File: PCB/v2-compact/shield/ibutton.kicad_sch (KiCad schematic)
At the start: 0 parts

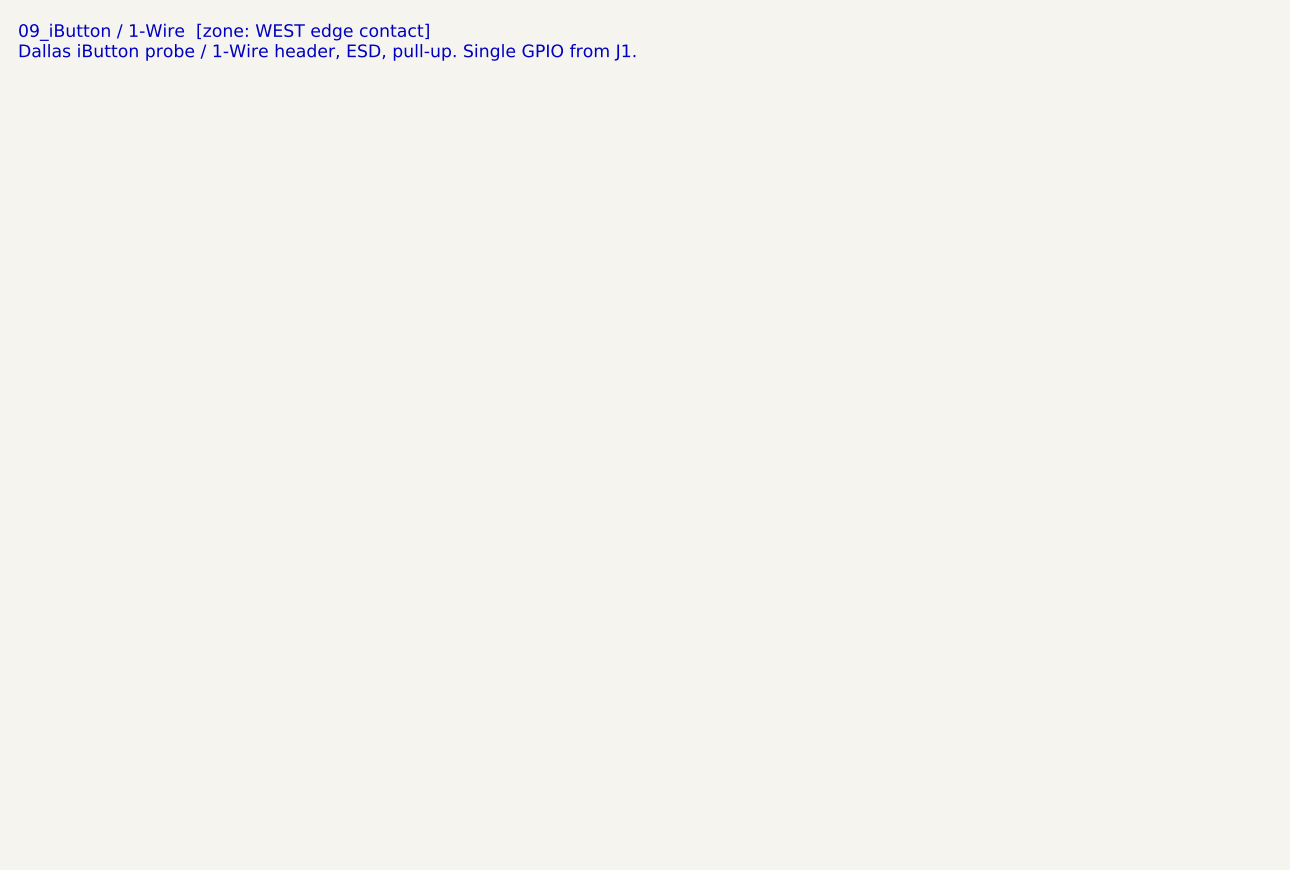
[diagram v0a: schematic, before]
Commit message: Schematics: custom symbols + footprint lib + backbone/nRF24/iButton sheets
- Add SnowOwl.kicad_sym (nRF24 + CC1101 module symbols; MISO tri-state for the
  shared SPI bus) and SnowOwl.pretty with the 2x10 stack-header footprint,
  registered via project sym-lib-table / fp-lib-table on both boards.
- Capture sheets, each netlist- and ERC-checked:
  - J1 stack header (both boards) wired to the locked pinout (the interconnect
    backbone: power + I2C + S3<->C5 UART + S3<->RV1106 UART + IR + 1-Wire)
  - nRF24 x3 on the shared SPI spine (per-radio CE/CSN/IRQ) with decoupling
  - iButton 1-Wire with pull-up
- Engine: snap all placements to the 1.27mm grid (clears 103 off-grid warnings);
  globally-unique power-symbol refs.

Remaining ERC items are expected for a partial design (isolated labels resolve
when both ends of a net are captured; power-not-driven clears with the power sheet).
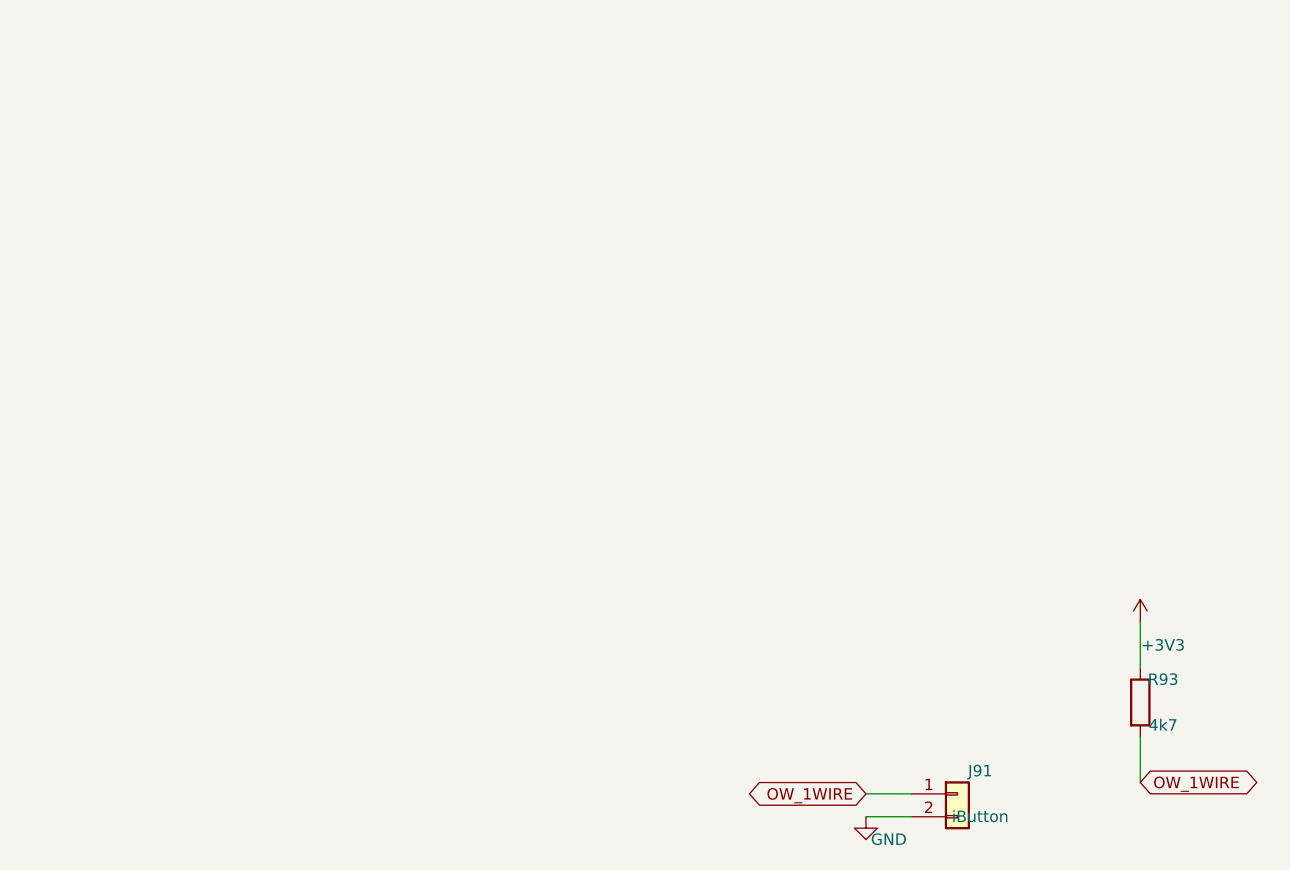
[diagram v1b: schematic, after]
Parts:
- added J91: iButton, Connector_PinHeader_2.54mm:PinHeader_1x02_P2.54mm_Vertical, symbol Connector_Generic:Conn_01x02
- added R93: 4k7, Resistor_SMD:R_0402_1005Metric, symbol Device:R
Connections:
- new net +3V3: R93.1
- new net GND: J91.2 (Pin_2)
- new net OW_1WIRE: J91.1 (Pin_1), R93.2
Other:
- note removed: "09_iButton / 1-Wire [zone: WEST edge contact] Dallas iButton probe / 1-Wire header, ESD, pull-up. Single GPIO from J1."
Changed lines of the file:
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@@
   (paper "A4")
   (title_block (title "09_iButton_1Wire") (company "YurilLAB"))
-  (text "09_iButton / 1-Wire  [zone: WEST edge contact]
-Dallas iButton probe / 1-Wire header, ESD, pull-up. Single GPIO from J1." (at 15 15 0)
-    (effects (font (size 1.4 1.4)) (justify left top)))
+  (symbol (lib_id "Connector_Generic:Conn_01x02") (at 119.38 100.33 0) (unit 1)
+    (in_bom yes) (on_board yes) (dnp no)
+    (property "Reference" "J91" (at 121.92 97.79 0) (effects (font (size 1.27 1.27))))
+    (property "Value" "iButton" (at 121.92 102.87 0) (effects (font (size 1.27 1.27))))
+    (property "Footprint" "Connector_PinHeader_2.54mm:PinHeader_1x02_P2.54mm_Vertical" (at 119.38 100.33 0) (effects (font (size 1.27 1.27)) hide))
+    (pin "1")
+    (pin "2")
+    (instances (project "SnowOwl-Shield" (path "/0a27d683-2113-42a8-9290-a545f7865850" (reference "J91") (unit 1))))
+  )
+  (wire (pts (xy 114.3 100.33) (xy 109.22 100.33)) (stroke (width 0) (type default)))
+  (global_label "OW_1WIRE" (shape bidirectional) (at 109.22 100.33 180) (fields_autoplaced)
+    (effects (font (size 1.27 1.27)) (justify right)))
+  (wire (pts (xy 114.3 102.87) (xy 109.22 102.87)) (stroke (width 0) (type default)))
+  (symbol (lib_id "power:GND") (at 109.22 102.87 0) (unit 1)
+    (in_bom yes) (on_board yes) (dnp no)
+    (property "Reference" "#PWR2424630" (at 111.76 100.33 0) (effects (font (size 1.27 1.27)) hide))
+    (property "Value" "GND" (at 111.76 105.41 0) (effects (font (size 1.27 1.27))))
+    (property "Footprint" "" (at 109.22 102.87 0) (effects (font (size 1.27 1.27)) hide))
+    (pin "1")
+    (instances (project "SnowOwl-Shield" (path "/0a27d683-2113-42a8-9290-a545f7865850" (reference "#PWR2424630") (unit 1))))
+  )
+  (symbol (lib_id "Device:R") (at 139.7 90.17 0) (unit 1)
+    (in_bom yes) (on_board yes) (dnp no)
+    (property "Reference" "R93" (at 142.24 87.63 0) (effects (font (size 1.27 1.27))))
+    (property "Value" "4k7" (at 142.24 92.71 0) (effects (font (size 1.27 1.27))))
+    (property "Footprint" "Resistor_SMD:R_0402_1005Metric" (at 139.7 90.17 0) (effects (font (size 1.27 1.27)) hide))
+    (pin "1")
+    (pin "2")
+    (instances (project "SnowOwl-Shield" (path "/0a27d683-2113-42a8-9290-a545f7865850" (reference "R93") (unit 1))))
+  )
+  (wire (pts (xy 139.7 86.36) (xy 139.7 81.28)) (stroke (width 0) (type default)))
+  (symbol (lib_id "power:+3V3") (at 139.7 81.28 0) (unit 1)
+    (in_bom yes) (on_board yes) (dnp no)
+    (property "Reference" "#PWRB23B192" (at 142.24 78.74 0) (effects (font (size 1.27 1.27)) hide))
+    (property "Value" "+3V3" (at 142.24 83.82 0) (effects (font (size 1.27 1.27))))
+    (property "Footprint" "" (at 139.7 81.28 0) (effects (font (size 1.27 1.27)) hide))
+    (pin "1")
+    (instances (project "SnowOwl-Shield" (path "/0a27d683-2113-42a8-9290-a545f7865850" (reference "#PWRB23B192") (unit 1))))
+  )
+  (wire (pts (xy 139.7 93.98) (xy 139.7 99.06)) (stroke (width 0) (type default)))
+  (global_label "OW_1WIRE" (shape bidirectional) (at 139.7 99.06 0) (fields_autoplaced)
+    (effects (font (size 1.27 1.27)) (justify left)))
   (sheet_instances (path "/" (page "1")))
 )
